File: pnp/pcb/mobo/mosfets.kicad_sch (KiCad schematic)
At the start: 0 parts

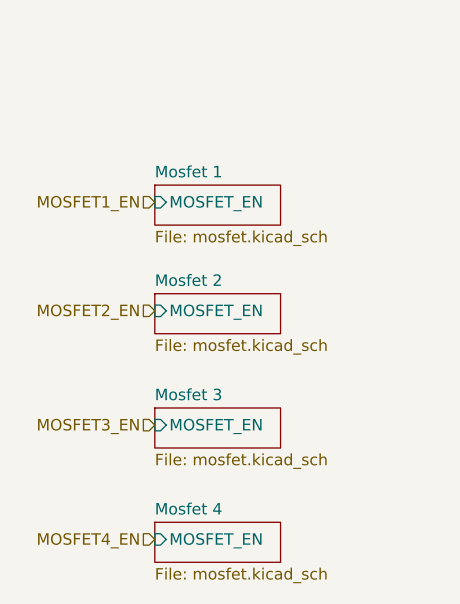
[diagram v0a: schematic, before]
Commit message: All sheets cleaned up
All symbols and their fields are now neatly organized.

All hierarchical pins are already imported,
except for the microcontroller sheet.
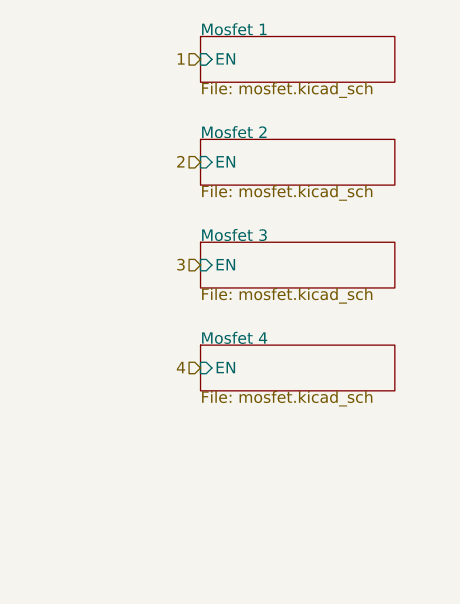
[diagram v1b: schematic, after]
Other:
- sheet Mosfet 1 ports: added EN; removed MOSFET_EN
- sheet Mosfet 2 ports: added EN; removed MOSFET_EN
- sheet Mosfet 3 ports: added EN; removed MOSFET_EN
- sheet Mosfet 4 ports: added EN; removed MOSFET_EN
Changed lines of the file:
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@@
 (kicad_sch (version 20211123) (generator eeschema)
   (paper "A4")
-  (hierarchical_label "MOSFET3_EN" (shape input) (at 135.89 120.65 180)
+  (hierarchical_label "3" (shape input) (at 140.97 102.87 180)
     (effects (font (size 1.27 1.27)) (justify right))
   )
-  (hierarchical_label "MOSFET2_EN" (shape input) (at 135.89 107.95 180)
+  (hierarchical_label "2" (shape input) (at 140.97 91.44 180)
     (effects (font (size 1.27 1.27)) (justify right))
   )
-  (hierarchical_label "MOSFET1_EN" (shape input) (at 135.89 95.885 180)
+  (hierarchical_label "1" (shape input) (at 140.97 80.01 180)
     (effects (font (size 1.27 1.27)) (justify right))
   )
-  (hierarchical_label "MOSFET4_EN" (shape input) (at 135.89 133.35 180)
+  (hierarchical_label "4" (shape input) (at 140.97 114.3 180)
     (effects (font (size 1.27 1.27)) (justify right))
   )
-  (sheet (at 135.89 131.445) (size 13.97 4.445) (fields_autoplaced)
+  (sheet (at 140.97 111.76) (size 21.59 5.08)
     (stroke (width 0) (type solid) (color 0 0 0 0))
     (fill (color 0 0 0 0.0000))
-    (property "Sheet name" "Mosfet 4" (id 0) (at 135.89 130.7334 0)
+    (property "Sheet name" "Mosfet 4" (id 0) (at 140.97 111.76 0)
       (effects (font (size 1.27 1.27)) (justify left bottom))
     )
-    (property "Sheet file" "mosfet.kicad_sch" (id 1) (at 135.89 136.4746 0)
+    (property "Sheet file" "mosfet.kicad_sch" (id 1) (at 140.97 116.84 0)
       (effects (font (size 1.27 1.27)) (justify left top))
     )
-    (pin "MOSFET_EN" input (at 135.89 133.35 180)
+    (pin "EN" input (at 140.97 114.3 180)
       (effects (font (size 1.27 1.27)) (justify left))
     )
   )
-  (sheet (at 135.89 106.045) (size 13.97 4.445) (fields_autoplaced)
+  (sheet (at 140.97 88.9) (size 21.59 5.08)
     (stroke (width 0) (type solid) (color 0 0 0 0))
     (fill (color 0 0 0 0.0000))
-    (property "Sheet name" "Mosfet 2" (id 0) (at 135.89 105.3334 0)
+    (property "Sheet name" "Mosfet 2" (id 0) (at 140.97 88.9 0)
       (effects (font (size 1.27 1.27)) (justify left bottom))
     )
-    (property "Sheet file" "mosfet.kicad_sch" (id 1) (at 135.89 111.0746 0)
+    (property "Sheet file" "mosfet.kicad_sch" (id 1) (at 140.97 93.98 0)
       (effects (font (size 1.27 1.27)) (justify left top))
     )
-    (pin "MOSFET_EN" input (at 135.89 107.95 180)
+    (pin "EN" input (at 140.97 91.44 180)
       (effects (font (size 1.27 1.27)) (justify left))
     )
   )
-  (sheet (at 135.89 118.745) (size 13.97 4.445) (fields_autoplaced)
+  (sheet (at 140.97 100.33) (size 21.59 5.08)
     (stroke (width 0) (type solid) (color 0 0 0 0))
     (fill (color 0 0 0 0.0000))
-    (property "Sheet name" "Mosfet 3" (id 0) (at 135.89 118.0334 0)
+    (property "Sheet name" "Mosfet 3" (id 0) (at 140.97 100.33 0)
       (effects (font (size 1.27 1.27)) (justify left bottom))
     )
-    (property "Sheet file" "mosfet.kicad_sch" (id 1) (at 135.89 123.7746 0)
+    (property "Sheet file" "mosfet.kicad_sch" (id 1) (at 140.97 105.41 0)
       (effects (font (size 1.27 1.27)) (justify left top))
     )
-    (pin "MOSFET_EN" input (at 135.89 120.65 180)
+    (pin "EN" input (at 140.97 102.87 180)
       (effects (font (size 1.27 1.27)) (justify left))
     )
   )
-  (sheet (at 135.89 93.98) (size 13.97 4.445) (fields_autoplaced)
+  (sheet (at 140.97 77.47) (size 21.59 5.08)
     (stroke (width 0) (type solid) (color 0 0 0 0))
     (fill (color 0 0 0 0.0000))
-    (property "Sheet name" "Mosfet 1" (id 0) (at 135.89 93.2684 0)
+    (property "Sheet name" "Mosfet 1" (id 0) (at 140.97 77.47 0)
       (effects (font (size 1.27 1.27)) (justify left bottom))
     )
-    (property "Sheet file" "mosfet.kicad_sch" (id 1) (at 135.89 99.0096 0)
+    (property "Sheet file" "mosfet.kicad_sch" (id 1) (at 140.97 82.55 0)
       (effects (font (size 1.27 1.27)) (justify left top))
     )
-    (pin "MOSFET_EN" input (at 135.89 95.885 180)
+    (pin "EN" input (at 140.97 80.01 180)
       (effects (font (size 1.27 1.27)) (justify left))
     )

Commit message: moving mobo-rev04b0 into mobo-rev04 branch from old repo
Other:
- company: (none) -> Opulo
- title: (none) -> LumenPnP Motherboard
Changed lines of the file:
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@@
   (paper "A4")
   (title_block
+    (title "LumenPnP Motherboard")
     (date "2022-03-29")
+    (company "Opulo")
   )
   (hierarchical_label "3" (shape input) (at 140.97 102.87 180)

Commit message: All pages checked
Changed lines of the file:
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@@
 (kicad_sch (version 20230121) (generator eeschema)
-  (paper "A4")
+  (paper "A5")
   (title_block
     (title "LumenPnP Motherboard")
@@
     (rev "005")
     (company "Opulo")
+    (comment 1 "MOSFETs")
   )
-  (hierarchical_label "3" (shape input) (at 140.97 102.87 180) (fields_autoplaced)
+  (hierarchical_label "3" (shape input) (at 92.71 77.47 180) (fields_autoplaced)
     (effects (font (size 1.27 1.27)) (justify right))
   )
-  (hierarchical_label "2" (shape input) (at 140.97 91.44 180) (fields_autoplaced)
+  (hierarchical_label "2" (shape input) (at 92.71 66.04 180) (fields_autoplaced)
     (effects (font (size 1.27 1.27)) (justify right))
   )
-  (hierarchical_label "1" (shape input) (at 140.97 80.01 180) (fields_autoplaced)
+  (hierarchical_label "1" (shape input) (at 92.71 54.61 180) (fields_autoplaced)
     (effects (font (size 1.27 1.27)) (justify right))
   )
-  (hierarchical_label "4" (shape input) (at 140.97 114.3 180) (fields_autoplaced)
+  (hierarchical_label "4" (shape input) (at 92.71 88.9 180) (fields_autoplaced)
     (effects (font (size 1.27 1.27)) (justify right))
   )
-  (sheet (at 140.97 111.76) (size 21.59 5.08)
+  (sheet (at 92.71 86.36) (size 21.59 5.08)
     (stroke (width 0) (type solid))
     (fill (color 0 0 0 0.0000))
-    (property "Sheetname" "Mosfet 4" (at 140.97 111.76 0)
+    (property "Sheetname" "Mosfet 4" (at 92.71 86.36 0)
       (effects (font (size 1.27 1.27)) (justify left bottom))
     )
-    (property "Sheetfile" "mosfet.kicad_sch" (at 140.97 116.84 0)
+    (property "Sheetfile" "mosfet.kicad_sch" (at 92.71 91.44 0)
       (effects (font (size 1.27 1.27)) (justify left top))
     )
-    (pin "EN" input (at 140.97 114.3 180)
+    (pin "EN" input (at 92.71 88.9 180)
       (effects (font (size 1.27 1.27)) (justify left))
     )
@@
     )
   )
-  (sheet (at 140.97 88.9) (size 21.59 5.08)
+  (sheet (at 92.71 63.5) (size 21.59 5.08)
     (stroke (width 0) (type solid))
     (fill (color 0 0 0 0.0000))
-    (property "Sheetname" "Mosfet 2" (at 140.97 88.9 0)
+    (property "Sheetname" "Mosfet 2" (at 92.71 63.5 0)
       (effects (font (size 1.27 1.27)) (justify left bottom))
     )
-    (property "Sheetfile" "mosfet.kicad_sch" (at 140.97 93.98 0)
+    (property "Sheetfile" "mosfet.kicad_sch" (at 92.71 68.58 0)
       (effects (font (size 1.27 1.27)) (justify left top))
     )
-    (pin "EN" input (at 140.97 91.44 180)
+    (pin "EN" input (at 92.71 66.04 180)
       (effects (font (size 1.27 1.27)) (justify left))
     )
@@
     )
   )
-  (sheet (at 140.97 100.33) (size 21.59 5.08)
+  (sheet (at 92.71 74.93) (size 21.59 5.08)
     (stroke (width 0) (type solid))
     (fill (color 0 0 0 0.0000))
-    (property "Sheetname" "Mosfet 3" (at 140.97 100.33 0)
+    (property "Sheetname" "Mosfet 3" (at 92.71 74.93 0)
       (effects (font (size 1.27 1.27)) (justify left bottom))
     )
-    (property "Sheetfile" "mosfet.kicad_sch" (at 140.97 105.41 0)
+    (property "Sheetfile" "mosfet.kicad_sch" (at 92.71 80.01 0)
       (effects (font (size 1.27 1.27)) (justify left top))
     )
-    (pin "EN" input (at 140.97 102.87 180)
+    (pin "EN" input (at 92.71 77.47 180)
       (effects (font (size 1.27 1.27)) (justify left))
     )
@@
     )
   )
-  (sheet (at 140.97 77.47) (size 21.59 5.08)
+  (sheet (at 92.71 52.07) (size 21.59 5.08)
     (stroke (width 0) (type solid))
     (fill (color 0 0 0 0.0000))
-    (property "Sheetname" "Mosfet 1" (at 140.97 77.47 0)
+    (property "Sheetname" "Mosfet 1" (at 92.71 52.07 0)
       (effects (font (size 1.27 1.27)) (justify left bottom))
     )
-    (property "Sheetfile" "mosfet.kicad_sch" (at 140.97 82.55 0)
+    (property "Sheetfile" "mosfet.kicad_sch" (at 92.71 57.15 0)
       (effects (font (size 1.27 1.27)) (justify left top))
     )
-    (pin "EN" input (at 140.97 80.01 180)
+    (pin "EN" input (at 92.71 54.61 180)
       (effects (font (size 1.27 1.27)) (justify left))
     )
